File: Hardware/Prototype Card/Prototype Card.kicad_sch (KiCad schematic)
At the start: 9 parts, among them J1 Conn_02x20_Odd_Even, J2 Conn_02x04_Odd_Even, U1 74LS138

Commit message: Cleanup
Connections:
- net R~{W} renamed RWB
- net RWB: now also CONN1.RWB; no longer CONN1.R~{W}
- net ~{IRQ} renamed IRQB
- net IRQB: now also CONN1.IRQB; no longer CONN1.~{IRQ}
- net ~{ML} renamed MLB
- net MLB: now also CONN1.MLB; no longer CONN1.~{ML}
- net ~{NMI} renamed NMIB
- net NMIB: now also CONN1.NMIB; no longer CONN1.~{NMI}
- net ~{RES} renamed RESB
- net RESB: now also CONN1.RESB; no longer CONN1.~{RES}
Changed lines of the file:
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@@
 		)
 	)
-	(label "~{NMI}"
+	(label "NMIB"
 		(at 93.98 50.8 0)
 		(fields_autoplaced yes)
@@
 		)
 	)
-	(label "~{NMI}"
+	(label "NMIB"
 		(at 35.56 50.8 0)
 		(fields_autoplaced yes)
@@
 		)
 	)
-	(label "~{ML}"
+	(label "MLB"
 		(at 35.56 60.96 0)
 		(fields_autoplaced yes)
@@
 		)
 	)
-	(label "~{ML}"
+	(label "MLB"
 		(at 93.98 60.96 0)
 		(fields_autoplaced yes)
@@
 		)
 	)
-	(label "~{IRQ}"
+	(label "IRQB"
 		(at 35.56 48.26 0)
 		(fields_autoplaced yes)
@@
 		)
 	)
-	(label "R~{W}"
+	(label "RWB"
 		(at 93.98 58.42 0)
 		(fields_autoplaced yes)
@@
 		)
 	)
-	(label "~{IRQ}"
+	(label "IRQB"
 		(at 93.98 48.26 0)
 		(fields_autoplaced yes)
@@
 		)
 	)
-	(label "R~{W}"
+	(label "RWB"
 		(at 35.56 58.42 0)
 		(fields_autoplaced yes)
@@
 		)
 	)
-	(label "~{RES}"
+	(label "RESB"
 		(at 93.98 45.72 0)
 		(fields_autoplaced yes)
@@
 		)
 	)
-	(label "~{RES}"
+	(label "RESB"
 		(at 35.56 45.72 0)
 		(fields_autoplaced yes)
@@
 		(pin "RDY"
 		)
-		(pin "R~{W}"
+		(pin "IRQB"
 		)
 		(pin "VCC"
@@
 		(pin "VCC"
 		)
-		(pin "~{IRQ}"
-		)
-		(pin "~{ML}"
-		)
-		(pin "~{NMI}"
-		)
-		(pin "~{RES}"
+		(pin "MLB"
+		)
+		(pin "NMIB"
+		)
+		(pin "RESB"
+		)
+		(pin "RWB"
 		)
 		(instances

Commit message: Updates
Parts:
- J1: footprint Connector_PinHeader_2.54mm:PinHeader_2x20_P2.54mm_Vertical -> Connector_PinSocket_2.54mm:PinSocket_2x20_P2.54mm_Vertical
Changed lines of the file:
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@@
 			)
 		)
-		(property "Footprint" "Connector_PinHeader_2.54mm:PinHeader_2x20_P2.54mm_Vertical"
+		(property "Footprint" "Connector_PinSocket_2.54mm:PinSocket_2x20_P2.54mm_Vertical"
 			(at 111.76 66.04 0)
 			(effects

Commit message: Working on new PCBs
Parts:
- B1, B2: footprint Prototype Card:BREADBOARD-MINI -> 6502 Parts:BREADBOARD-MINI; symbol Prototype_Card:BREADBOARDMINI -> 6502 Parts:BREADBOARDMINI
- J1: renamed from CONN1; footprint Prototype Card:6502CARDEDGE -> 6502 Parts:6502CARDEDGE; symbol Prototype_Card:6502CARDEDGE -> 6502 Parts:6502CARDEDGE
- renumbered C3 to C2, C2 to C3, J1 to J2, J2 to J3
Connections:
- net MLB renamed SYNC
- net SYNC: now also J1.SYNC; no longer J1.MLB
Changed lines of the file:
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@@
 		(title "6502 Prototype Card")
 		(date "2024-03-19")
-		(rev "2.0")
+		(rev "1.0")
 		(company "A.C. Wright Design")
 	)
@@
 		)
 	)
-	(label "MLB"
+	(label "SYNC"
 		(at 35.56 60.96 0)
 		(fields_autoplaced yes)
@@
 		)
 	)
-	(label "MLB"
+	(label "SYNC"
 		(at 93.98 60.96 0)
 		(fields_autoplaced yes)
@@
 	)
 	(symbol
-		(lib_id "Prototype_Card:BREADBOARDMINI")
+		(lib_id "6502 Parts:BREADBOARDMINI")
 		(at 137.16 187.96 0)
 		(unit 1)
@@
 			)
 		)
-		(property "Footprint" "Prototype Card:BREADBOARD-MINI"
+		(property "Footprint" "6502 Parts:BREADBOARD-MINI"
 			(at 137.16 187.96 0)
 			(effects
@@
 	)
 	(symbol
-		(lib_id "Prototype_Card:6502CARDEDGE")
+		(lib_id "6502 Parts:6502CARDEDGE")
 		(at 60.96 66.04 0)
 		(unit 1)
@@
 		(on_board yes)
 		(dnp no)
-		(property "Reference" "CONN1"
+		(property "Reference" "J1"
 			(at 60.96 36.2712 0)
 			(effects
@@
 			)
 		)
-		(property "Footprint" "Prototype Card:6502CARDEDGE"
+		(property "Footprint" "6502 Parts:6502CARDEDGE"
 			(at 60.96 66.04 0)
 			(effects
@@
 		(pin "VCC"
 		)
-		(pin "MLB"
+		(pin "SYNC"
 		)
 		(pin "NMIB"
@@
 			(project "Prototype Card"
 				(path "/1eb588e8-a8a6-45d4-8449-ed494748d485"
-					(reference "CONN1")
+					(reference "J1")
 					(unit 1)
 				)
@@
 		(on_board yes)
 		(dnp no)
-		(property "Reference" "J1"
+		(property "Reference" "J2"
 			(at 113.03 40.005 0)
 			(effects
@@
 			(project "Prototype Card"
 				(path "/1eb588e8-a8a6-45d4-8449-ed494748d485"
-					(reference "J1")
+					(reference "J2")
 					(unit 1)
 				)
@@
 		(on_board yes)
 		(dnp no)
-		(property "Reference" "J2"
+		(property "Reference" "J3"
 			(at 223.52 59.2582 0)
 			(effects
@@
 			(project "Prototype Card"
 				(path "/1eb588e8-a8a6-45d4-8449-ed494748d485"
-					(reference "J2")
+					(reference "J3")
 					(unit 1)
 				)
@@
 		(on_board yes)
 		(dnp no)
-		(property "Reference" "C3"
+		(property "Reference" "C2"
 			(at 113.03 95.1992 90)
 			(effects
@@
 			(project "Prototype Card"
 				(path "/1eb588e8-a8a6-45d4-8449-ed494748d485"
-					(reference "C3")
+					(reference "C2")
 					(unit 1)
 				)
@@
 		(on_board yes)
 		(dnp no)
-		(property "Reference" "C2"
+		(property "Reference" "C3"
 			(at 162.6108 68.58 90)
 			(effects
@@
 			(project "Prototype Card"
 				(path "/1eb588e8-a8a6-45d4-8449-ed494748d485"
-					(reference "C2")
+					(reference "C3")
 					(unit 1)
 				)
@@
 	)
 	(symbol
-		(lib_id "Prototype_Card:BREADBOARDMINI")
+		(lib_id "6502 Parts:BREADBOARDMINI")
 		(at 110.49 187.96 0)
 		(unit 1)
@@
 			)
 		)
-		(property "Footprint" "Prototype Card:BREADBOARD-MINI"
+		(property "Footprint" "6502 Parts:BREADBOARD-MINI"
 			(at 110.49 187.96 0)
 			(effects
@@
 		(dnp no)
 		(fields_autoplaced yes)
-		(property "Reference" "#FLG02"
+		(property "Reference" "#FLG01"
 			(at 188.595 44.45 0)
 			(effects
@@
 			(project "Prototype Card"
 				(path "/1eb588e8-a8a6-45d4-8449-ed494748d485"
-					(reference "#FLG02")
+					(reference "#FLG01")
 					(unit 1)
 				)
@@
 		(dnp no)
 		(fields_autoplaced yes)
-		(property "Reference" "#FLG01"
+		(property "Reference" "#FLG02"
 			(at 188.595 86.36 0)
 			(effects
@@
 			(project "Prototype Card"
 				(path "/1eb588e8-a8a6-45d4-8449-ed494748d485"
-					(reference "#FLG01")
+					(reference "#FLG02")
 					(unit 1)
 				)

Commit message: Add production files
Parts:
- B1, B2, J1, J2, J3: now left out of the parts list
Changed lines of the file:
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@@
 		(unit 1)
 		(exclude_from_sim no)
-		(in_bom yes)
+		(in_bom no)
 		(on_board yes)
 		(dnp no)
@@
 		(unit 1)
 		(exclude_from_sim no)
-		(in_bom yes)
+		(in_bom no)
 		(on_board yes)
 		(dnp no)
@@
 		(unit 1)
 		(exclude_from_sim no)
-		(in_bom yes)
+		(in_bom no)
 		(on_board yes)
 		(dnp no)
@@
 		(unit 1)
 		(exclude_from_sim no)
-		(in_bom yes)
+		(in_bom no)
 		(on_board yes)
 		(dnp no)
@@
 		(unit 1)
 		(exclude_from_sim no)
-		(in_bom yes)
-		(on_board yes)
-		(dnp no)
+		(in_bom no)
+		(on_board yes)
+		(dnp no)

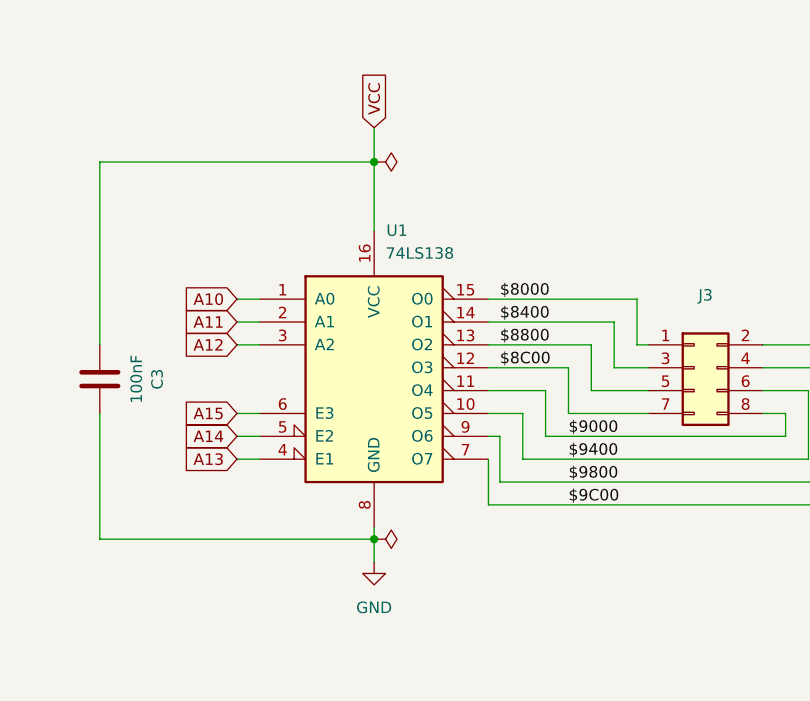
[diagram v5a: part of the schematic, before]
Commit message: Add GPIO cards
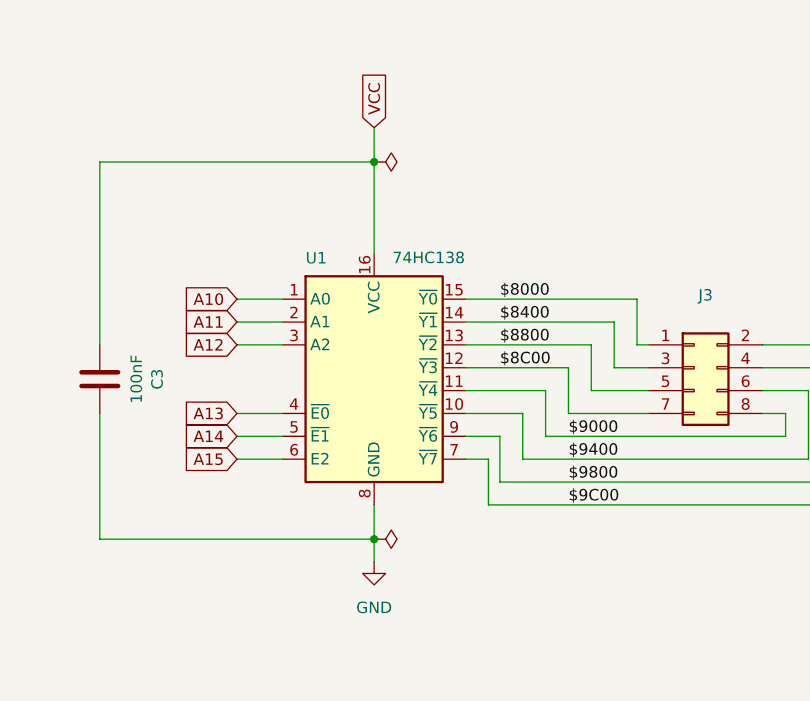
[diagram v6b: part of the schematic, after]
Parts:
- U1: value 74LS138 -> 74HC138; symbol 74xx:74LS138 -> 74xx:74HC138
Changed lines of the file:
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@@
 	(title_block
 		(title "6502 Prototype Card")
-		(date "2024-03-19")
+		(date "2024-06-05")
 		(rev "1.0")
 		(company "A.C. Wright Design")
@@
 	(wire
 		(pts
-			(xy 173.99 62.23) (xy 171.45 62.23)
+			(xy 171.45 62.23) (xy 176.53 62.23)
 		)
 		(stroke
@@
 	(wire
 		(pts
-			(xy 173.99 59.69) (xy 171.45 59.69)
+			(xy 171.45 59.69) (xy 176.53 59.69)
 		)
 		(stroke
@@
 	(wire
 		(pts
-			(xy 199.39 69.85) (xy 205.74 69.85)
+			(xy 196.85 67.31) (xy 208.28 67.31)
 		)
 		(stroke
@@
 	(wire
 		(pts
-			(xy 186.69 85.09) (xy 186.69 86.36)
+			(xy 186.69 82.55) (xy 186.69 86.36)
 		)
 		(stroke
@@
 		)
 	)
-	(wire
+	(bus
 		(pts
-			(xy 173.99 77.47) (xy 171.45 77.47)
+			(xy 90.17 68.58) (xy 90.17 71.12)
 		)
 		(stroke
@@
 		)
 	)
-	(bus
+	(wire
 		(pts
-			(xy 90.17 68.58) (xy 90.17 71.12)
+			(xy 133.35 58.42) (xy 119.38 58.42)
 		)
 		(stroke
@@
 	(wire
 		(pts
-			(xy 133.35 58.42) (xy 119.38 58.42)
+			(xy 34.29 63.5) (xy 45.72 63.5)
 		)
 		(stroke
@@
 	(wire
 		(pts
-			(xy 34.29 63.5) (xy 45.72 63.5)
+			(xy 210.82 69.85) (xy 217.17 69.85)
 		)
 		(stroke
@@
 	(wire
 		(pts
-			(xy 210.82 69.85) (xy 217.17 69.85)
+			(xy 121.92 91.44) (xy 133.35 91.44)
 		)
 		(stroke
@@
 	(wire
 		(pts
-			(xy 121.92 91.44) (xy 133.35 91.44)
+			(xy 196.85 69.85) (xy 205.74 69.85)
 		)
 		(stroke
@@
 	(wire
 		(pts
-			(xy 199.39 59.69) (xy 215.9 59.69)
+			(xy 76.2 68.58) (xy 87.63 68.58)
 		)
 		(stroke
@@
 	(wire
 		(pts
-			(xy 199.39 72.39) (xy 203.2 72.39)
+			(xy 45.72 45.72) (xy 34.29 45.72)
 		)
 		(stroke
@@
 		)
 	)
-	(wire
+	(bus
 		(pts
-			(xy 76.2 68.58) (xy 87.63 68.58)
+			(xy 31.75 68.58) (xy 31.75 71.12)
 		)
 		(stroke
@@
 	(wire
 		(pts
-			(xy 45.72 45.72) (xy 34.29 45.72)
+			(xy 196.85 62.23) (xy 213.36 62.23)
 		)
 		(stroke
@@
 	(bus
 		(pts
-			(xy 31.75 68.58) (xy 31.75 71.12)
+			(xy 31.75 109.22) (xy 90.17 109.22)
 		)
 		(stroke
@@
 		)
 	)
-	(bus
+	(wire
 		(pts
-			(xy 31.75 109.22) (xy 90.17 109.22)
+			(xy 196.85 77.47) (xy 199.39 77.47)
 		)
 		(stroke
@@
 	(wire
 		(pts
+			(xy 171.45 72.39) (xy 176.53 72.39)
+		)
+		(stroke
+			(width 0)
+			(type default)
+		)
+	)
+	(wire
+		(pts
 			(xy 119.38 60.96) (xy 133.35 60.96)
 		)
@@
 		)
 	)
+	(wire
+		(pts
+			(xy 196.85 64.77) (xy 210.82 64.77)
+		)
+		(stroke
+			(width 0)
+			(type default)
+		)
+	)
 	(bus
 		(pts
@@
 	(wire
 		(pts
-			(xy 199.39 67.31) (xy 208.28 67.31)
-		)
-		(stroke
-			(width 0)
-			(type default)
-		)
-	)
-	(wire
-		(pts
 			(xy 106.68 63.5) (xy 92.71 63.5)
 		)
@@
 	(wire
 		(pts
-			(xy 186.69 44.45) (xy 156.21 44.45)
+			(xy 196.85 74.93) (xy 200.66 74.93)
 		)
 		(stroke
@@
 	(wire
 		(pts
-			(xy 199.39 64.77) (xy 210.82 64.77)
+			(xy 186.69 44.45) (xy 156.21 44.45)
 		)
 		(stroke
@@
 	(wire
 		(pts
-			(xy 186.69 52.07) (xy 186.69 44.45)
+			(xy 186.69 54.61) (xy 186.69 44.45)
 		)
 		(stroke
@@
 	(wire
 		(pts
-			(xy 173.99 64.77) (xy 171.45 64.77)
+			(xy 171.45 64.77) (xy 176.53 64.77)
 		)
 		(stroke
@@
 	(wire
 		(pts
-			(xy 199.39 62.23) (xy 213.36 62.23)
-		)
-		(stroke
-			(width 0)
-			(type default)
-		)
-	)
-	(wire
-		(pts
 			(xy 133.35 63.5) (xy 119.38 63.5)
 		)
@@
 		)
 	)
-	(wire
-		(pts
-			(xy 199.39 74.93) (xy 200.66 74.93)
-		)
-		(stroke
-			(width 0)
-			(type default)
-		)
-	)
 	(bus
 		(pts
@@
 	(wire
 		(pts
-			(xy 173.99 74.93) (xy 171.45 74.93)
+			(xy 171.45 74.93) (xy 176.53 74.93)
+		)
+		(stroke
+			(width 0)
+			(type default)
+		)
+	)
+	(wire
+		(pts
+			(xy 196.85 59.69) (xy 215.9 59.69)
 		)
 		(stroke
@@
 		)
 	)
+	(wire
+		(pts
+			(xy 196.85 72.39) (xy 203.2 72.39)
+		)
+		(stroke
+			(width 0)
+			(type default)
+		)
+	)
 	(bus
 		(pts
@@
 	(wire
 		(pts
-			(xy 240.03 64.77) (xy 240.03 82.55)
+			(xy 171.45 77.47) (xy 176.53 77.47)
 		)
 		(stroke
@@
 	(wire
 		(pts
-			(xy 121.92 43.18) (xy 119.38 43.18)
+			(xy 240.03 64.77) (xy 240.03 82.55)
 		)
 		(stroke
@@
 	(wire
 		(pts
-			(xy 171.45 72.39) (xy 173.99 72.39)
+			(xy 121.92 43.18) (xy 119.38 43.18)
 		)
 		(stroke
@@
 	(global_label "A15"
 		(shape input)
-		(at 171.45 72.39 180)
+		(at 171.45 77.47 180)
 		(effects
 			(font
@@
 		)
 		(property "Intersheetrefs" "${INTERSHEET_REFS}"
-			(at 171.45 72.39 0)
+			(at 171.45 77.47 0)
 			(effects
 				(font
@@
 	(global_label "A13"
 		(shape input)
-		(at 171.45 77.47 180)
+		(at 171.45 72.39 180)
 		(effects
 			(font
@@
 		)
 		(property "Intersheetrefs" "${INTERSHEET_REFS}"
-			(at 171.45 77.47 0)
+			(at 171.45 72.39 0)
 			(effects
 				(font
@@
 	)
 	(symbol
-		(lib_id "74xx:74LS138")
-		(at 186.69 67.31 0)
+		(lib_id "74xx:74HC138")
+		(at 186.69 69.85 0)
 		(unit 1)
 		(exclude_from_sim no)
@@
 		(dnp no)
 		(property "Reference" "U1"
-			(at 189.23 52.07 0)
+			(at 179.07 55.88 0)
 			(effects
 				(font
 					(size 1.27 1.27)
 				)
+				(justify left bottom)
 			)
 		)
-		(property "Value" "74LS138"
-			(at 191.77 54.61 0)
+		(property "Value" "74HC138"
+			(at 188.722 54.356 0)
 			(effects
 				(font
 					(size 1.27 1.27)
 				)
+				(justify left top)
 			)
 		)
 		(property "Footprint" "Package_SO:SOIC-16_3.9x9.9mm_P1.27mm"
-			(at 186.69 67.31 0)
+			(at 186.69 69.85 0)
 			(effects
 				(font
@@
 			)
 		)
-		(property "Datasheet" "http://www.ti.com/lit/gpn/sn74LS138"
-			(at 186.69 67.31 0)
+		(property "Datasheet" "http://www.ti.com/lit/ds/symlink/cd74hc238.pdf"
+			(at 186.69 69.85 0)
 			(effects
 				(font
@@
 			)
 		)
-		(property "Description" ""
-			(at 186.69 67.31 0)
+		(property "Description" "3-to-8 line decoder/multiplexer inverting, DIP-16/SOIC-16/SSOP-16"
+			(at 186.69 69.85 0)
 			(effects
 				(font
@@
 		)
 		(property "LCSC" "C5602"
-			(at 186.69 67.31 0)
+			(at 186.69 69.85 0)
 			(effects
 				(font

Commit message: Cleanup
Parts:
- B1, B2: value BREADBOARDMINI -> Breadboard Mini; footprint 6502 Parts:BREADBOARD-MINI -> 6502 Parts:Breadboard Mini; symbol 6502 Parts:BREADBOARDMINI -> 6502 Parts:Breadboard Mini; now in the parts list
- J1: value 6502CARDEDGE -> 6502 Card Edge; footprint 6502 Parts:6502CARDEDGE -> 6502 Parts:6502 Card Edge; symbol 6502 Parts:6502CARDEDGE -> 6502 Parts:6502 Card Edge
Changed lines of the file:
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@@
 	(title_block
 		(title "6502 Prototype Card")
-		(date "2024-06-05")
+		(date "2024-06-12")
 		(rev "1.0")
 		(company "A.C. Wright Design")
@@
 	)
 	(bus_entry
+		(at 90.17 88.9)
+		(size -2.54 2.54)
+		(stroke
+			(width 0)
+			(type default)
+		)
+	)
+	(bus_entry
 		(at 31.75 83.82)
 		(size 2.54 2.54)
@@
 	)
 	(bus_entry
+		(at 90.17 40.64)
+		(size -2.54 2.54)
+		(stroke
+			(width 0)
+			(type default)
+		)
+	)
+	(bus_entry
 		(at 135.89 68.58)
 		(size -2.54 2.54)
@@
 	(wire
 		(pts
+			(xy 76.2 91.44) (xy 87.63 91.44)
+		)
+		(stroke
+			(width 0)
+			(type default)
+		)
+	)
+	(wire
+		(pts
 			(xy 121.92 91.44) (xy 121.92 101.6)
 		)
@@
 	(wire
 		(pts
+			(xy 76.2 43.18) (xy 87.63 43.18)
+		)
+		(stroke
+			(width 0)
+			(type default)
+		)
+	)
+	(wire
+		(pts
 			(xy 119.38 50.8) (xy 133.35 50.8)
 		)
@@
 	)
 	(label "GND"
+		(at 82.55 91.44 0)
+		(fields_autoplaced yes)
+		(effects
+			(font
+				(size 1.27 1.27)
+			)
+			(justify left bottom)
+		)
+	)
+	(label "GND"
 		(at 35.56 43.18 0)
 		(fields_autoplaced yes)
@@
 		)
 	)
+	(label "VCC"
+		(at 82.55 43.18 0)
+		(fields_autoplaced yes)
+		(effects
+			(font
+				(size 1.27 1.27)
+			)
+			(justify left bottom)
+		)
+	)
 	(label "A9"
 		(at 132.08 66.04 180)
@@
 	)
 	(symbol
-		(lib_id "6502 Parts:BREADBOARDMINI")
+		(lib_id "6502 Parts:Breadboard Mini")
 		(at 137.16 187.96 0)
 		(unit 1)
 		(exclude_from_sim no)
-		(in_bom no)
+		(in_bom yes)
 		(on_board yes)
 		(dnp no)
@@
 			)
 		)
-		(property "Value" "BREADBOARDMINI"
+		(property "Value" "Breadboard Mini"
 			(at 132.08 193.294 0)
 			(effects
@@
 			)
 		)
-		(property "Footprint" "6502 Parts:BREADBOARD-MINI"
+		(property "Footprint" "6502 Parts:Breadboard Mini"
 			(at 137.16 187.96 0)
 			(effects
@@
 	)
 	(symbol
-		(lib_id "6502 Parts:6502CARDEDGE")
+		(lib_id "6502 Parts:6502 Card Edge")
 		(at 60.96 66.04 0)
 		(unit 1)
@@
 		(dnp no)
 		(property "Reference" "J1"
-			(at 60.96 36.2712 0)
+			(at 50.546 37.338 0)
 			(effects
 				(font
 					(size 1.4986 1.4986)
 				)
+				(justify left bottom)
 			)
 		)
-		(property "Value" "6502CARDEDGE"
-			(at 60.96 38.7604 0)
+		(property "Value" "6502 Card Edge"
+			(at 58.42 38.862 0)
 			(effects
 				(font
@@
 			)
 		)
-		(property "Footprint" "6502 Parts:6502CARDEDGE"
+		(property "Footprint" "6502 Parts:6502 Card Edge"
 			(at 60.96 66.04 0)
 			(effects
@@
 		(dnp no)
 		(property "Reference" "U1"
-			(at 179.07 55.88 0)
+			(at 188.976 52.832 0)
 			(effects
 				(font
@@
 	)
 	(symbol
-		(lib_id "6502 Parts:BREADBOARDMINI")
+		(lib_id "6502 Parts:Breadboard Mini")
 		(at 110.49 187.96 0)
 		(unit 1)
 		(exclude_from_sim no)
-		(in_bom no)
+		(in_bom yes)
 		(on_board yes)
 		(dnp no)
@@
 			)
 		)
-		(property "Value" "BREADBOARDMINI"
+		(property "Value" "Breadboard Mini"
 			(at 105.41 193.294 0)
 			(effects
@@
 			)
 		)
-		(property "Footprint" "6502 Parts:BREADBOARD-MINI"
+		(property "Footprint" "6502 Parts:Breadboard Mini"
 			(at 110.49 187.96 0)
 			(effects
